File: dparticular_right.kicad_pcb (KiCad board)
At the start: 2 copper layers, 185.7 x 157.2 mm, 51 parts, among them J1 To Left Hand, SW1:10 Key_Ins, SW1:11 Key_Prnt, SW2:10 Key_F7, SW2:11 Key_F8, SW2:12 Key_F9, SW2:13 Key_F10, SW2:14 Key_F11, SW2:15 Key_F12, SW2:16 Key_Del, SW3:10 Key_7, SW3:11 Key_8, SW3:12 Key_9, SW3:13 Key_0, SW3:14 Key_Hyph, SW3:15 Key_Eql, SW3:16 Key_Bksp, SW3:9 Key_6, SW4:10 Key_U, SW4:11 Key_I, SW4:12 Key_O, SW4:13 Key_P, SW4:14 Key_LBrk, SW4:15 Key_RBrk, SW4:16 Key_BkSl, SW4:9 Key_Y, SW5:10 Key_J, SW5:11 Key_K, SW5:12 Key_L, SW5:13 Key_Semi, SW5:14 Key_Quot, SW5:16 Key_Entr, SW5:9 Key_H, SW6:10 Key_M, SW6:11 Key_Coma, SW6:12 Key_Per, SW6:13 Key_Slsh, SW6:14 Key_RShft, SW6:9 Key_N, SW7:11 Key_RAlt, SW7:12 Key_RWin, SW7:13 Key_Menu, SW7:14 Key_RCtrl, SW7:9 Key_RSpc, U1 MCP23018

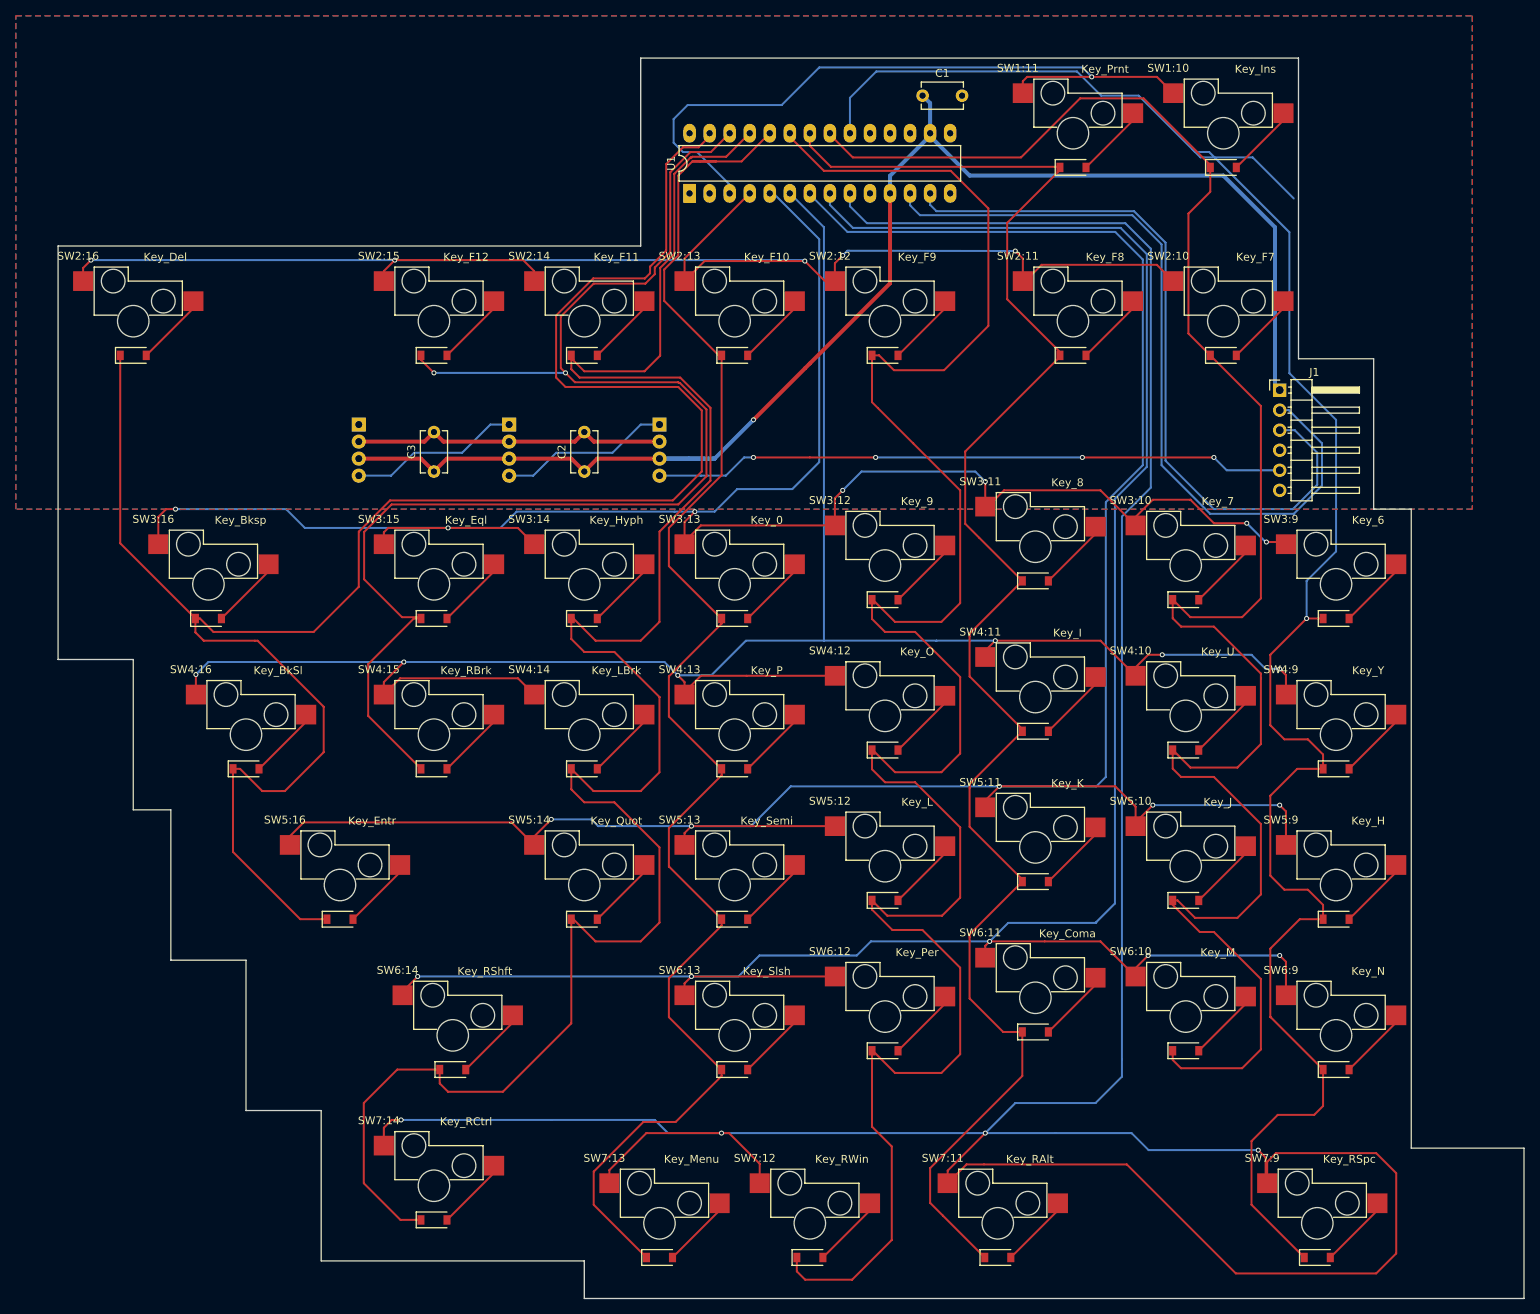
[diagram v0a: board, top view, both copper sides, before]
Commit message: Right Hand PCB: Make some space for potential future drill holes
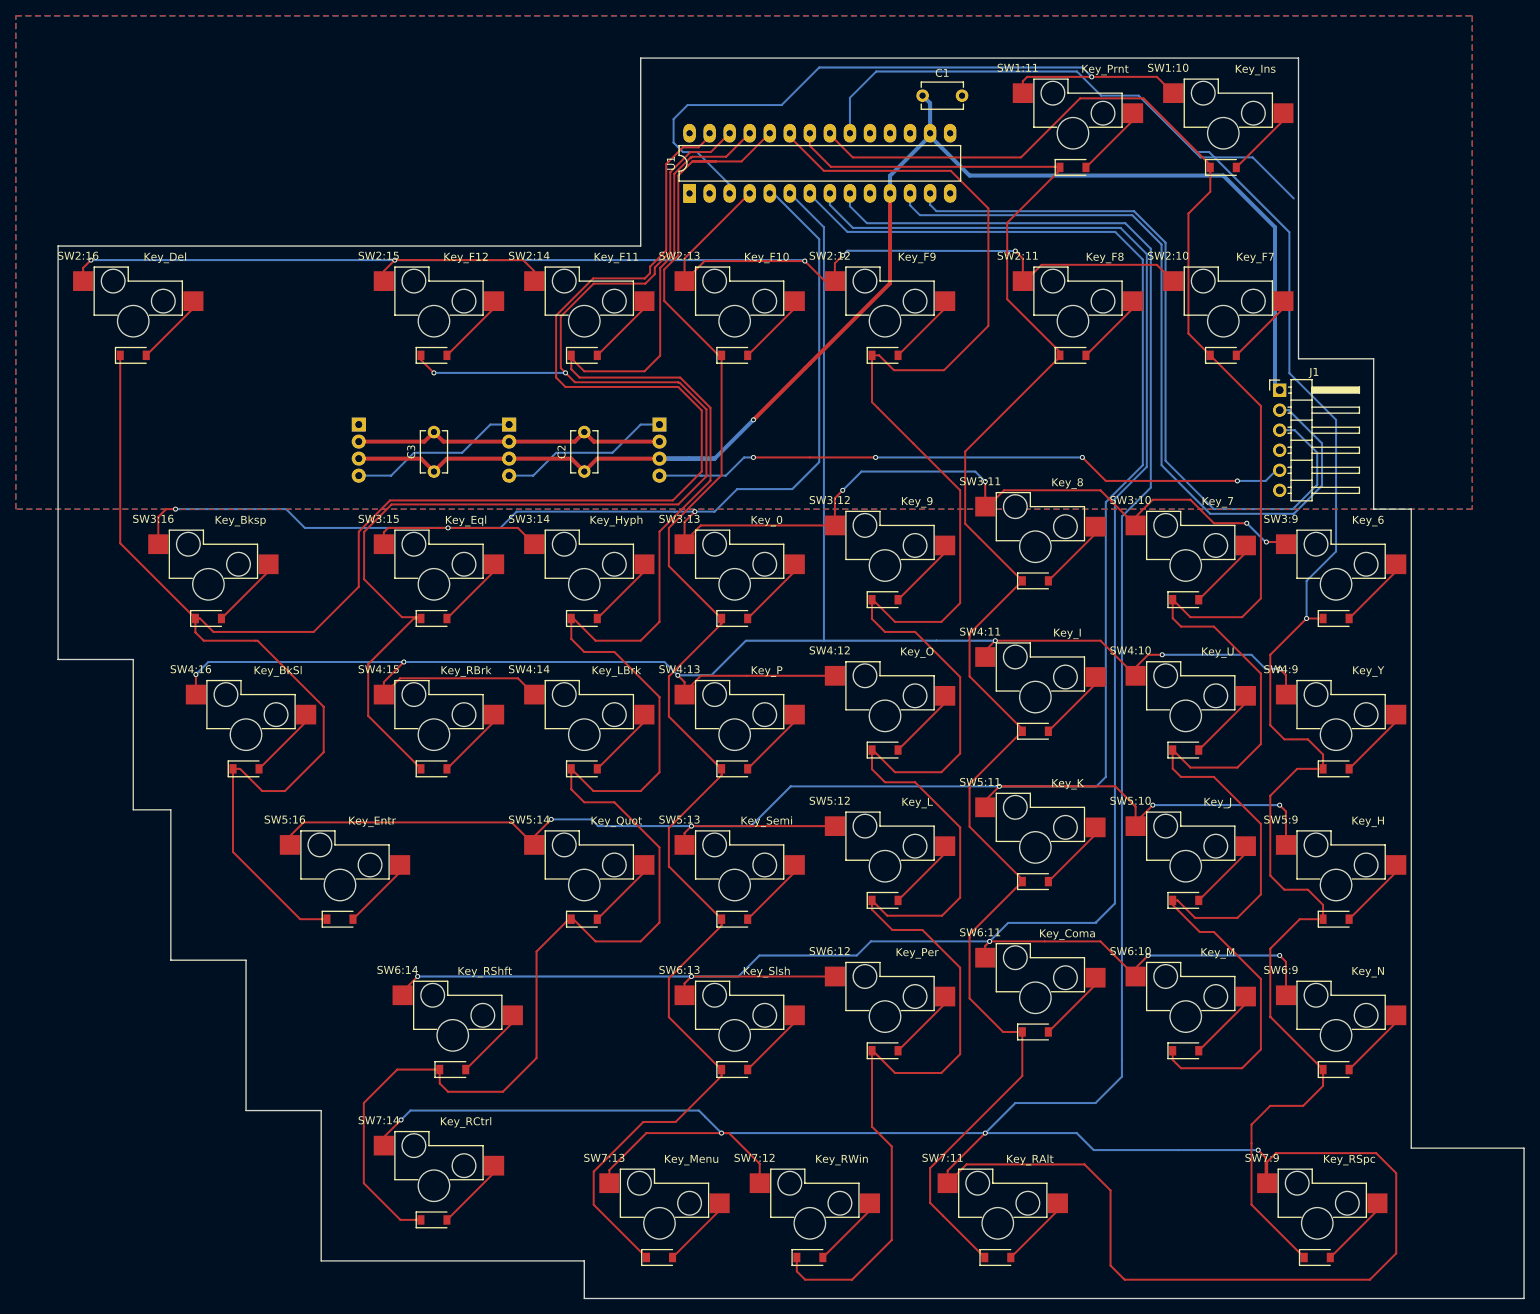
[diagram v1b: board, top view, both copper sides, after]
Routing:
- net /ROW7: track 418.7 -> 425.3 mm
- net /LED_D: track 80.2 -> 81.3 mm

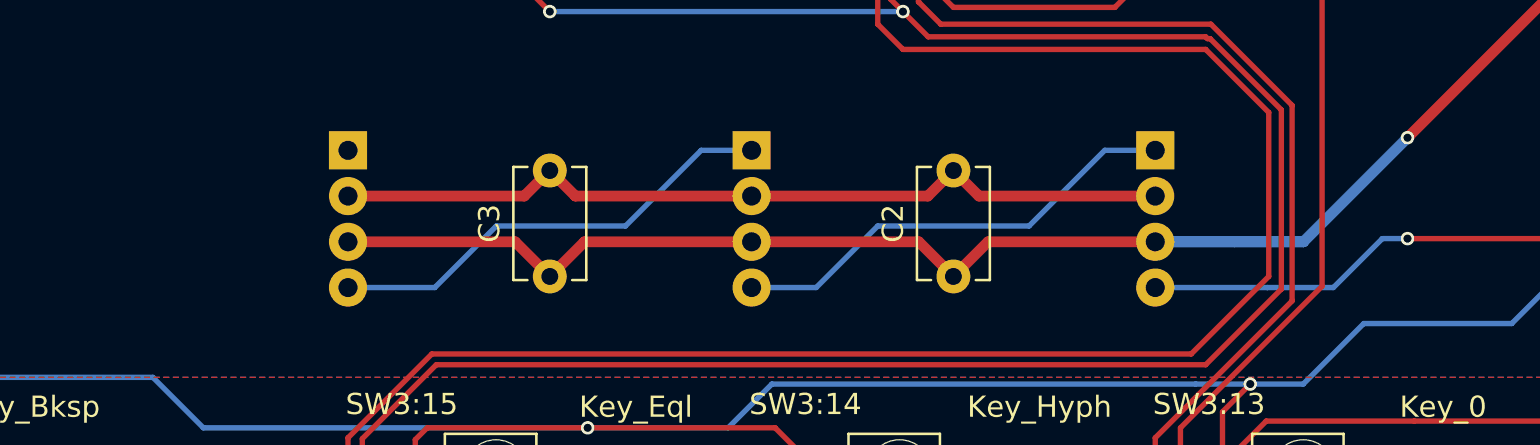
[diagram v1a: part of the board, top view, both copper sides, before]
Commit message: Right Hand PCB: Moved LEDs half a key right and centered them vertically
I made this change after discovering that, head on in perspective view,
the LEDs are more visible centered on the keys than on the key edges.
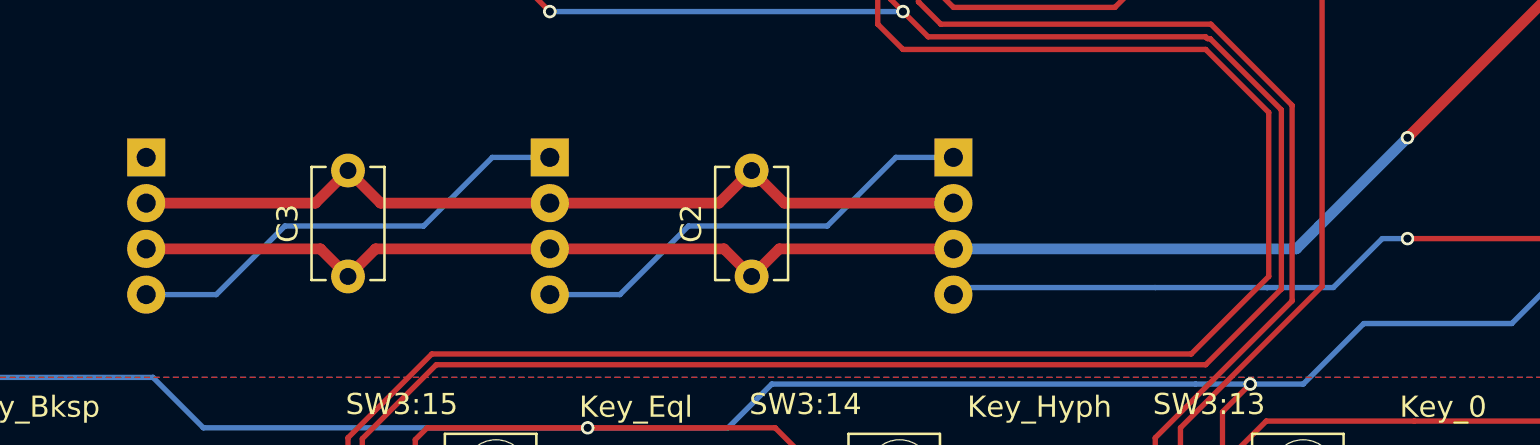
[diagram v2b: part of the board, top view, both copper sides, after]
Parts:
- moved D2 9.53 mm to (76.2, 70.6)
- moved D3 9.53 mm to (57.2, 70.6)
- moved D1 9.53 mm to (95.3, 70.6)
- moved C2 9.52 mm to (85.7, 76.2)
- moved C3 9.52 mm to (66.7, 76.2)
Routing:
- net /LED_D: track 81.3 -> 90.9 mm
- net +5V: track 182.2 -> 184.3 mm
- net GND: track 40.1 -> 40.7 mm
